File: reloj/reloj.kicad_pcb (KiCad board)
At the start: 2 copper layers, 50 x 50 mm, 15 parts, among them J1 Barrel_Jack, J2 Barrel_Jack, J3 Conn_01x02, U1 NE555P

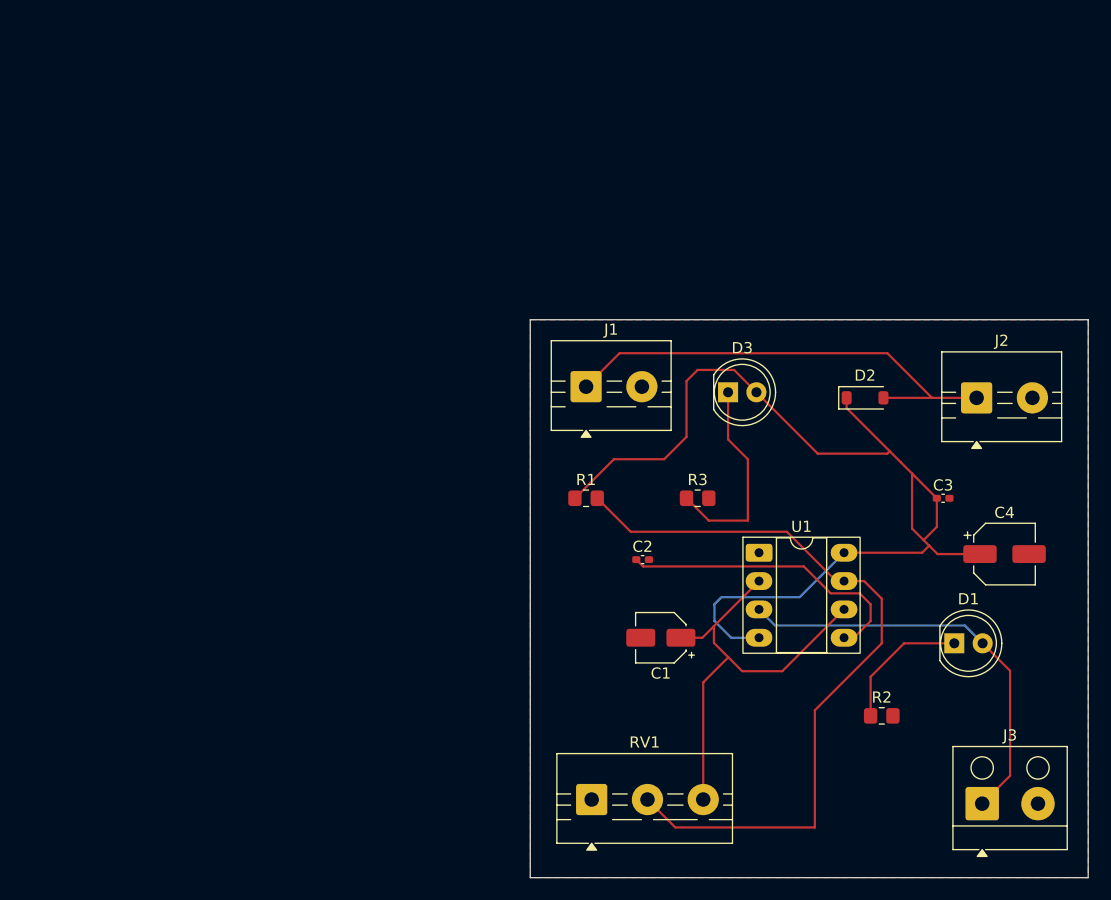
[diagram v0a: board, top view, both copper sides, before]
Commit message: convertir de a4 a a5
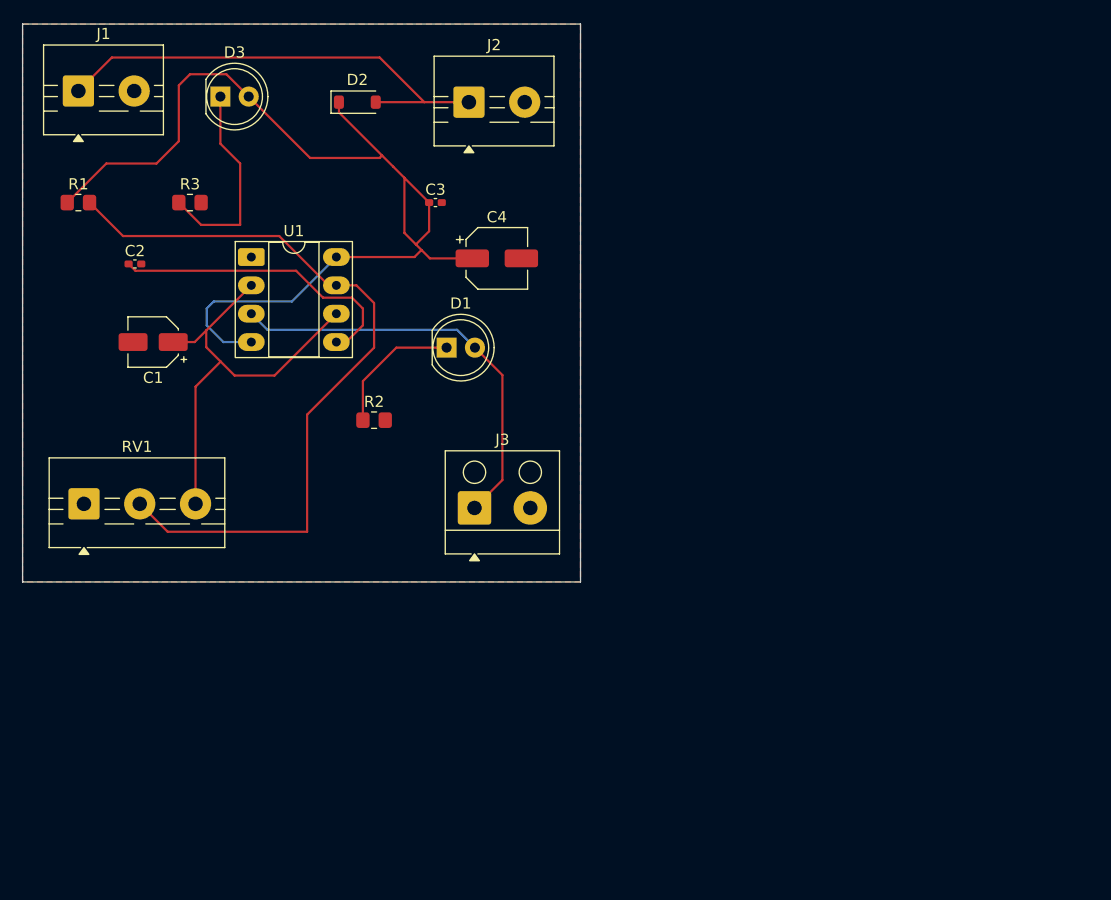
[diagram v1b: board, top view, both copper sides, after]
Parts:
- moved C1 52.7 mm to (66.2, 102.0)
- moved C2 52.7 mm to (64.6, 95.0)
- moved C3 52.7 mm to (91.5, 89.5)
- moved C4 52.7 mm to (97.0, 94.5)
- moved D1 52.7 mm to (92.5, 102.5)
- moved D2 52.7 mm to (84.5, 80.5)
- moved D3 52.7 mm to (72.2, 80.0)
- moved J1 52.7 mm to (59.5, 79.5)
- moved J2 52.7 mm to (94.5, 80.5)
- moved J3 52.7 mm to (95.0, 116.9)
- moved R1 52.7 mm to (59.5, 89.5)
- moved R2 52.7 mm to (86.0, 109.0)
- moved R3 52.7 mm to (69.5, 89.5)
- moved RV1 52.7 mm to (60.0, 116.5)
- moved U1 52.7 mm to (75.0, 94.4)
